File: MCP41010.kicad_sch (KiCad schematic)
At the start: 4 parts, among them U15 MCP41010

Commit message: Add LORA, SDcard and Volt to 4_20mA scheamtic
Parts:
- renumbered C36 to C40, R102 to R118, R103 to R119, U15 to U21
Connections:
- net MCP41010.CS renamed MCP41010.CS_MCP41010
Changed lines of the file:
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@@
 		)
 	)
-	(label "MCP41010.CS"
+	(label "MCP41010.CS_MCP41010"
 		(at 99.06 99.06 180)
 		(fields_autoplaced yes)
@@
 		)
 	)
-	(label "MCP41010.CS"
-		(at 130.175 85.09 180)
-		(fields_autoplaced yes)
-		(effects
-			(font
-				(size 1.27 1.27)
-			)
-			(justify right bottom)
-		)
-	)
 	(label "MCP41010.SCK"
 		(at 130.175 80.01 180)
+		(fields_autoplaced yes)
+		(effects
+			(font
+				(size 1.27 1.27)
+			)
+			(justify right bottom)
+		)
+	)
+	(label "MCP41010.CS_MCP41010"
+		(at 130.175 85.09 180)
 		(fields_autoplaced yes)
 		(effects
@@
 		)
 	)
-	(hierarchical_label "MCP41010{SPI}"
+	(hierarchical_label "MCP41010{ST_SPI2}"
 		(shape input)
 		(at 110.49 91.44 0)
@@
 		(on_board yes)
 		(dnp no)
-		(property "Reference" "U15"
+		(property "Reference" "U21"
 			(at 134.62 72.39 0)
 			(effects
@@
 			(project "DongTamV2"
 				(path "/2303d546-b88a-4ab0-aee1-26e3b32ac9d7/c44414d4-f62b-4b90-ad16-4c8725291991/c600683c-bdbc-4b87-a874-b1d5badfcacc"
-					(reference "U15")
+					(reference "U21")
 					(unit 1)
 				)
@@
 		(dnp no)
 		(fields_autoplaced yes)
-		(property "Reference" "C36"
+		(property "Reference" "C40"
 			(at 128.27 60.96 90)
 			(effects
@@
 			(project "DongTamV2"
 				(path "/2303d546-b88a-4ab0-aee1-26e3b32ac9d7/c44414d4-f62b-4b90-ad16-4c8725291991/c600683c-bdbc-4b87-a874-b1d5badfcacc"
-					(reference "C36")
+					(reference "C40")
 					(unit 1)
 				)
@@
 		(on_board yes)
 		(dnp no)
-		(property "Reference" "R103"
+		(property "Reference" "R119"
 			(at 152.4 92.71 90)
 			(effects
@@
 			(project "DongTamV2"
 				(path "/2303d546-b88a-4ab0-aee1-26e3b32ac9d7/c44414d4-f62b-4b90-ad16-4c8725291991/c600683c-bdbc-4b87-a874-b1d5badfcacc"
-					(reference "R103")
+					(reference "R119")
 					(unit 1)
 				)
@@
 		(on_board yes)
 		(dnp no)
-		(property "Reference" "R102"
+		(property "Reference" "R118"
 			(at 152.4 71.12 90)
 			(effects
@@
 			(project "DongTamV2"
 				(path "/2303d546-b88a-4ab0-aee1-26e3b32ac9d7/c44414d4-f62b-4b90-ad16-4c8725291991/c600683c-bdbc-4b87-a874-b1d5badfcacc"
-					(reference "R102")
+					(reference "R118")
 					(unit 1)
 				)

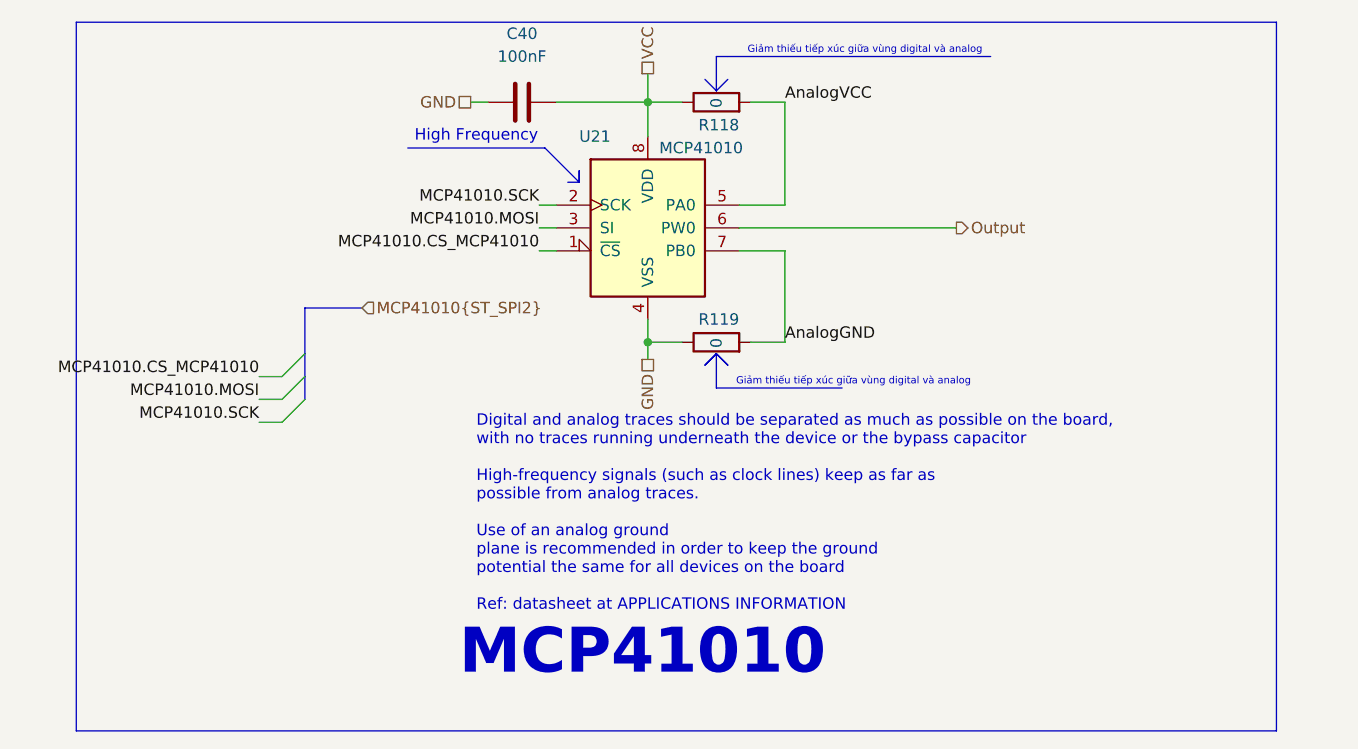
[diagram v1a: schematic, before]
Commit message: Layout p2, fix Analog VCC and GND for opamp circuit
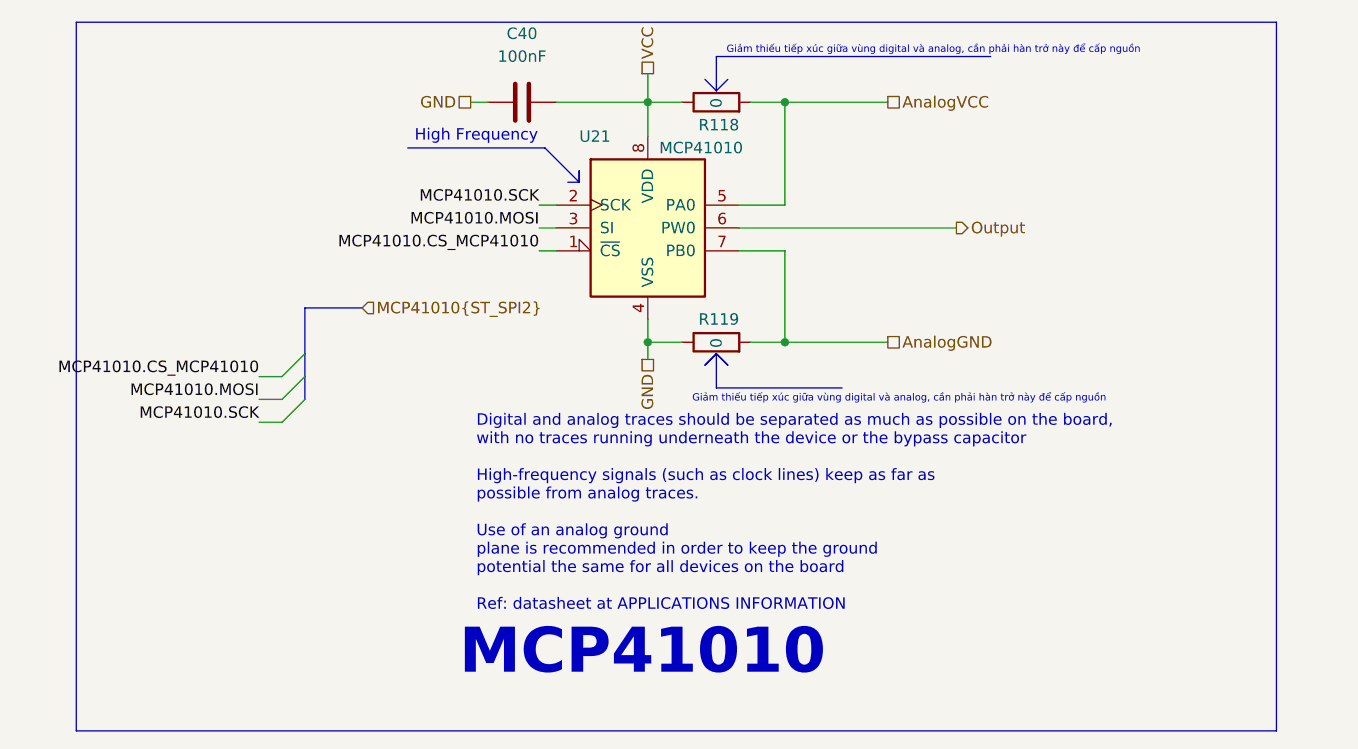
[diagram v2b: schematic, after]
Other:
- note added: "Giảm thiếu tiếp xúc giữa vùng digital và analog, cần phải hàn trở này để cấp nguồn"
- note removed: "Giảm thiếu tiếp xúc giữa vùng digital và analog"
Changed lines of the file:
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@@
+		(color 0 0 0 0)
+	)
+	(junction
+		(at 157.48 68.58)
+		(diameter 0)
+		(color 0 0 0 0)
+	)
+	(junction
+		(at 157.48 95.25)
+		(diameter 0)
 		(color 0 0 0 0)
 	)
@@
 		)
 	)
+	(wire
+		(pts
+			(xy 157.48 85.09) (xy 157.48 95.25)
+		)
+		(stroke
+			(width 0)
+			(type default)
+		)
+	)
 	(polyline
 		(pts
@@
 	(wire
 		(pts
+			(xy 157.48 68.58) (xy 168.91 68.58)
+		)
+		(stroke
+			(width 0)
+			(type default)
+		)
+	)
+	(wire
+		(pts
 			(xy 152.4 82.55) (xy 176.53 82.55)
 		)
@@
 	(wire
 		(pts
+			(xy 157.48 95.25) (xy 168.91 95.25)
+		)
+		(stroke
+			(width 0)
+			(type default)
+		)
+	)
+	(wire
+		(pts
 			(xy 130.175 85.09) (xy 132.08 85.09)
 		)
@@
 		(pts
 			(xy 148.59 97.79) (xy 149.86 96.52)
-		)
-		(stroke
-			(width 0)
-			(type default)
-		)
-	)
-	(wire
-		(pts
-			(xy 157.48 85.09) (xy 157.48 95.25)
 		)
 		(stroke
@@
 		)
 	)
-	(text "Giảm thiếu tiếp xúc giữa vùng digital và analog "
+	(text "Giảm thiếu tiếp xúc giữa vùng digital và analog, cần phải hàn trở này để cấp nguồn"
 		(exclude_from_sim no)
-		(at 166.37 62.865 0)
+		(at 173.99 62.865 0)
 		(effects
 			(font
@@
 		)
 	)
-	(text "Giảm thiếu tiếp xúc giữa vùng digital và analog "
+	(text "Giảm thiếu tiếp xúc giữa vùng digital và analog, cần phải hàn trở này để cấp nguồn"
 		(exclude_from_sim no)
-		(at 165.1 99.695 0)
+		(at 170.18 101.6 0)
 		(effects
 			(font
@@
 		)
 	)
-	(label "AnalogGND"
-		(at 157.48 95.25 0)
-		(fields_autoplaced yes)
-		(effects
-			(font
-				(size 1.27 1.27)
-			)
-			(justify left bottom)
-		)
-	)
 	(label "MCP41010.SCK"
 		(at 130.175 80.01 180)
@@
 		)
 	)
-	(label "AnalogVCC"
-		(at 157.48 68.58 0)
-		(fields_autoplaced yes)
-		(effects
-			(font
-				(size 1.27 1.27)
-			)
-			(justify left bottom)
+	(hierarchical_label "AnalogGND"
+		(shape passive)
+		(at 168.91 95.25 0)
+		(fields_autoplaced yes)
+		(effects
+			(font
+				(size 1.27 1.27)
+			)
+			(justify left)
 		)
 	)
@@
 		)
 	)
+	(hierarchical_label "AnalogVCC"
+		(shape passive)
+		(at 168.91 68.58 0)
+		(fields_autoplaced yes)
+		(effects
+			(font
+				(size 1.27 1.27)
+			)
+			(justify left)
+		)
+	)
